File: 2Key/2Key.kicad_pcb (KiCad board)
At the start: 2 copper layers, 20 parts, among them SW1 SW_Push, U1 ATmega32U4-A, Y1 16MHz

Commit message: l
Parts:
- C1, C2, C3, C4, C5, C6, C7, F1, R1, R2, R3, R4, R5, R6, SW1, U1, USB1, Y1: moved to B.Cu
- moved R2 61.2 mm to (159.5, 65.1), turned to -90 degrees
- moved R3 60.5 mm to (162.7, 65.1), turned to -90 degrees
- moved F1 42.8 mm to (175.4, 101.6), turned to 180 degrees
- moved C3 37.2 mm to (179.0, 132.5), turned to 180 degrees
- moved C6 35.1 mm to (169.1, 101.0), turned to -90 degrees
- moved R4 30.1 mm to (151.6, 98.4), turned to -90 degrees
- moved C1 28.6 mm to (146.1, 99.9), turned to 180 degrees
- moved C2 28.6 mm to (146.1, 108.6), turned to 0 degrees
- moved Y1 28.6 mm to (146.1, 103.8), turned to 180 degrees
- moved R1 27.2 mm to (146.7, 123.2), turned to 180 degrees
- moved C4 26.0 mm to (173.3, 132.2), turned to 180 degrees
- moved C7 25.4 mm to (169.9, 108.0), turned to 90 degrees
- moved R5 18.4 mm to (151.2, 129.1), turned to 180 degrees
- moved R6 9.57 mm to (155.6, 129.2), turned to 180 degrees
- moved USB1 2.25 mm to (160.3, 55.6)
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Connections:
- C6 pad 1: +5V -> VCC
- C7 pad 1: +5V -> VCC
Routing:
- net Net-(R3-Pad2): track 0.00 -> 45.8 mm, vias 0 -> 2
- net Net-(R2-Pad2): track 0.00 -> 45.5 mm, vias 0 -> 2
- net Net-(R4-Pad2): track 0.00 -> 25.1 mm, vias 0 -> 2
- net Net-(C1-Pad2): track 0.00 -> 25.0 mm
- net GND: track 0.00 -> 24.5 mm
- net Net-(C2-Pad2): track 0.00 -> 11.8 mm
- net VCC: track 0.00 -> 7.22 mm
- net +5V: track 0.00 -> 3.67 mm

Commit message: Save Progress
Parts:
- added D1: WS2812B, LED_SMD:LED_WS2812B-2020_PLCC4_2.0x2.0mm, B.Cu at (169.9, 85.7)
- added D2: WS2812B, LED_SMD:LED_WS2812B-2020_PLCC4_2.0x2.0mm, F.Cu at (181.0, 112.7)
- added R7: 5.1k, Resistor_SMD:R_0805_2012Metric, B.Cu at (167.5, 61.1)
- added R8: 5.1k, Resistor_SMD:R_0805_2012Metric, B.Cu at (153.3, 61.1)
- added U2: PRTR5V0U2X, Package_TO_SOT_SMD:SOT-143, B.Cu at (160.3, 67.5)
- USB1: value Molex-0548190589 -> HRO-TYPE-C-31-M-12; footprint Connector_USB:USB_Micro-B_Molex-105133-0031 -> Type-C:HRO-TYPE-C-31-M-12-Assembly
- moved C3 46.2 mm to (154.0, 93.7), turned to 90 degrees
- moved R6 42.7 mm to (169.9, 88.9)
- moved R5 41.0 mm to (150.7, 88.1)
- moved F1 37.7 mm to (165.9, 65.1), turned to -90 degrees
- moved R1 33.7 mm to (166.7, 96.0), turned to 90 degrees
- moved C4 20.5 mm to (164.9, 113.5)
- moved R2 7.32 mm to (158.0, 72.2)
- moved R3 7.14 mm to (162.7, 72.2)
- moved USB1 3.37 mm to (160.3, 52.2)
- moved C5 0.65 mm to (160.3, 113.5)
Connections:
- C6 pad 1: VCC -> +5V
- C7 pad 1: VCC -> +5V
- MX1 pad 2: Net-(R5-Pad2) -> Net-(MX1-Pad2)
- MX2 pad 2: Net-(R6-Pad2) -> Net-(MX2-Pad2)
- R5 pad 2: Net-(R5-Pad2) -> Net-(MX1-Pad2)
- R6 pad 2: Net-(R6-Pad2) -> Net-(MX2-Pad2)
- U1 pad 25: unconnected-(U1-Pad25) -> Net-(MX1-Pad2)
- U1 pad 26: unconnected-(U1-Pad26) -> RGBLED
- U1 pad 32: unconnected-(U1-Pad32) -> Net-(MX2-Pad2)
- U1 pad 8: Net-(R5-Pad2) -> unconnected-(U1-Pad8)
- U1 pad 9: Net-(R6-Pad2) -> unconnected-(U1-Pad9)
- USB1 pad 2: unconnected-(USB1-Pad2) -> VCC
- USB1 pad 3: D+ -> unconnected-(USB1-Pad3)
- USB1 pad 4: D- -> Net-(R8-Pad1)
- USB1 pad 5: VCC -> D-
- USB1 pad 6: unconnected-(USB1-Pad6) -> D+
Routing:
- net +5V: track 3.67 -> 162.5 mm, vias 0 -> 4
- net Net-(MX2-Pad2): track 0.00 -> 32.5 mm, vias 0 -> 2
- net D+: track 0.00 -> 27.5 mm, vias 0 -> 2
- net Net-(MX1-Pad2): track 0.00 -> 26.2 mm, vias 0 -> 2
- net D-: track 0.00 -> 25.8 mm, vias 0 -> 4
- net Net-(R2-Pad2): track 45.5 -> 24.5 mm
- net VCC: track 7.22 -> 26.3 mm, vias 0 -> 3
- net Net-(C3-Pad1): track 0.00 -> 18.5 mm, vias 0 -> 2
- net Net-(R8-Pad1): track 0.00 -> 11.5 mm
- net Net-(R7-Pad1): track 0.00 -> 11.1 mm
- net Net-(R3-Pad2): track 45.8 -> 38.0 mm
- net GND: track 24.5 -> 29.5 mm
- net Net-(R1-Pad1): track 0.00 -> 3.23 mm

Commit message: Save Progress
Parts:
- D2: moved to B.Cu
- moved D2 29.2 mm to (169.9, 85.7), turned to 180 degrees
- moved D1 19.2 mm to (150.7, 85.7)
- moved R5 0.79 mm to (150.7, 88.9)
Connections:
- U1 pad 14: VCC -> +5V
- U1 pad 2: VCC -> +5V
- U1 pad 24: VCC -> +5V
- U1 pad 44: VCC -> +5V
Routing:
- net Net-(D1-Pad2): track 0.00 -> 20.2 mm, vias 0 -> 6
- net RGBLED: track 0.00 -> 19.5 mm, vias 0 -> 2
- net GND: track 29.5 -> 44.4 mm, vias 0 -> 3
- net Net-(R2-Pad2): track 24.5 -> 39.0 mm
- net Net-(MX1-Pad2): track 26.2 -> 35.5 mm
- net +5V: track 162.5 -> 153.9 mm, vias 4 -> 2
- net Net-(R3-Pad2): track 38.0 -> 38.6 mm

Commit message: Updated PCB
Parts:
- added C8: 0.1uF, Capacitor_SMD:C_0805_2012Metric, B.Cu at (151.2, 109.0)
- added C9: 0.1uF, Capacitor_SMD:C_0805_2012Metric, B.Cu at (153.8, 96.8)
- MX1, MX2: moved to B.Cu
- moved C3 20.0 mm to (156.8, 113.5), turned to 180 degrees
- moved R4 1.11 mm to (150.5, 98.5)
- turned MX1 to 180 degrees
- turned MX2 to 180 degrees
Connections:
- U1 pad 34: VCC -> +5V
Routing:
- net GND: track 44.4 -> 119.4 mm, vias 3 -> 14
- net +5V: track 153.9 -> 180.0 mm, vias 2 -> 6
- net Net-(C3-Pad1): track 18.5 -> 5.59 mm
- net Net-(MX2-Pad2): track 32.5 -> 28.4 mm, vias 2 -> 3
- net Net-(R4-Pad2): track 25.1 -> 27.1 mm
- net VCC: track 26.3 -> 27.2 mm
- net D-: track 25.8 -> 25.0 mm
- net Net-(R3-Pad2): track 38.6 -> 39.3 mm
- net Net-(MX1-Pad2): track 35.5 -> 35.6 mm, vias 2 -> 3
- added copper zone on B.Cu, net GND
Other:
- board outline added: 49.2 x 71.4 mm

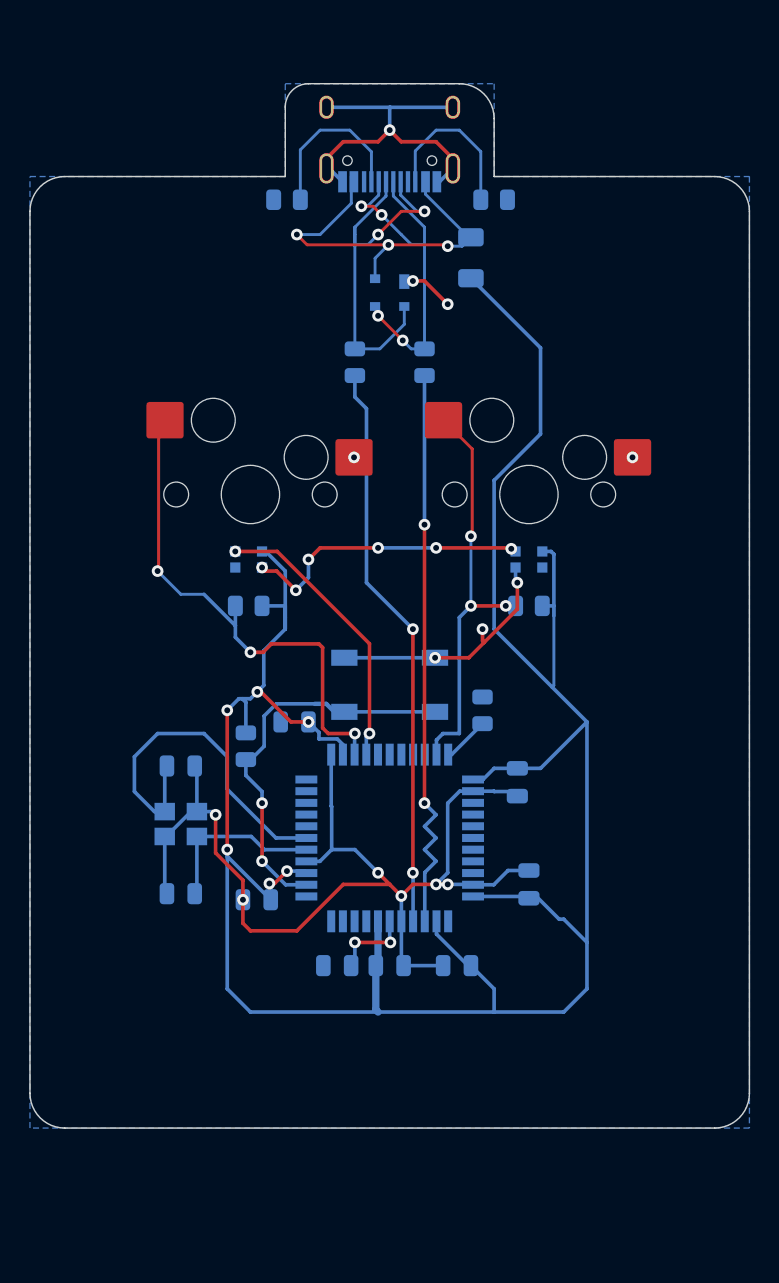
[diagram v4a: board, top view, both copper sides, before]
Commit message: Remade PCB with the MU Chip
Remade the PCB with the MU Chip and switched to reverse mounted LEDs
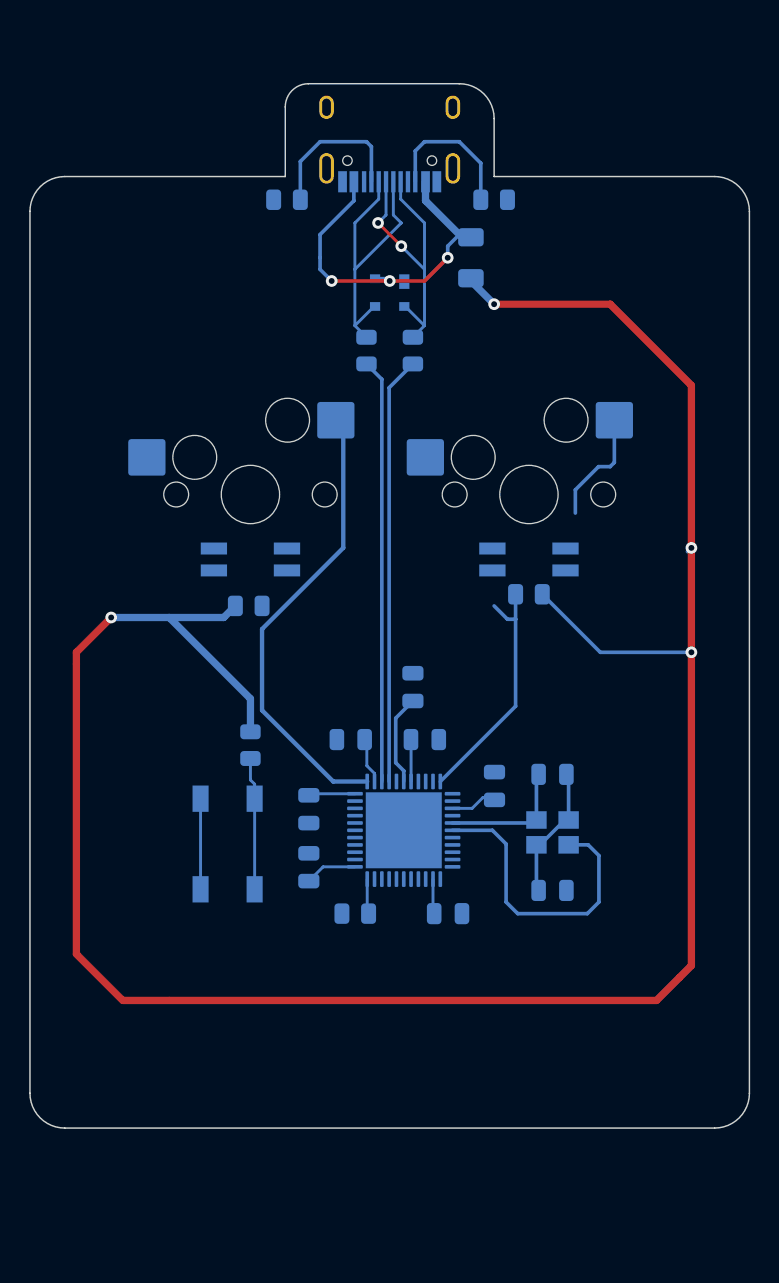
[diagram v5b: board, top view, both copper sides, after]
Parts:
- C3: value C_Small -> 1uF
- D1, D2: value WS2812B -> SK6812MINI; footprint LED_SMD:LED_WS2812B-2020_PLCC4_2.0x2.0mm -> LED:SK6812MINIE
- MX1, MX2: moved to F.Cu
- U1: value ATmega32U4-A -> ATmega32U4-M; footprint Package_QFP:TQFP-44_10x10mm_P0.8mm -> Package_DFN_QFN:QFN-44-1EP_7x7mm_P0.5mm_EP5.2x5.2mm
- moved C1 26.8 mm to (171.5, 108.4), turned to 0 degrees
- moved C2 26.7 mm to (171.5, 100.4), turned to 180 degrees
- moved Y1 25.4 mm to (171.5, 104.4), turned to 0 degrees
- moved C3 19.7 mm to (161.9, 94.5), turned to 90 degrees
- moved R1 16.4 mm to (158.0, 110.0), turned to 180 degrees
- moved C7 15.9 mm to (154.8, 102.8), turned to -90 degrees
- moved C5 15.6 mm to (162.7, 98.0)
- moved SW1 15.5 mm to (149.2, 105.2), turned to -90 degrees
- moved C9 14.4 mm to (167.5, 101.2), turned to 90 degrees
- moved C6 11.8 mm to (157.7, 98.0), turned to 180 degrees
- moved C8 4.19 mm to (154.8, 106.8), turned to 90 degrees
- moved R2 4.05 mm to (161.9, 71.4)
- moved R3 4.05 mm to (158.8, 71.4)
- moved C4 3.61 mm to (164.3, 110.0), turned to 0 degrees
- moved U1 1.10 mm to (161.3, 104.2), turned to -90 degrees
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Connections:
- D1 pad 1: +5V -> Net-(D1-Pad1)
- D1 pad 2: Net-(D1-Pad2) -> GND
- D1 pad 3: GND -> RGBLED
- D1 pad 4: RGBLED -> +5V
- D2 pad 1: +5V -> unconnected-(D2-Pad1)
- D2 pad 2: unconnected-(D2-Pad2) -> GND
- D2 pad 3: GND -> Net-(D1-Pad1)
- D2 pad 4: Net-(D1-Pad2) -> +5V
- U1 pad 1: unconnected-(U1-Pad1) -> Net-(MX2-Pad2)
- U1 pad 11: unconnected-(U1-Pad11) -> Net-(MX1-Pad2)
- U1 pad 14: +5V -> VCC
- U1 pad 2: +5V -> VCC
- U1 pad 24: +5V -> VCC
- U1 pad 25: Net-(MX1-Pad2) -> unconnected-(U1-Pad25)
- U1 pad 32: Net-(MX2-Pad2) -> unconnected-(U1-Pad32)
- U1 pad 34: +5V -> VCC
- U1 pad 44: +5V -> VCC
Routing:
- net GND: track 119.4 -> 15.5 mm, vias 14 -> 0
- net Net-(D1-Pad2): track 20.2 -> 0.00 mm, vias 6 -> 0
- net RGBLED: track 19.5 -> 0.00 mm, vias 2 -> 0
- net Net-(R4-Pad2): track 27.1 -> 9.07 mm, vias 2 -> 0
- net +5V: track 180.0 -> 165.9 mm, vias 6 -> 4
- net Net-(R3-Pad2): track 39.3 -> 29.0 mm, vias 2 -> 0
- net Net-(R2-Pad2): track 39.0 -> 29.2 mm, vias 2 -> 0
- net VCC: track 27.2 -> 35.9 mm
- net D+: track 27.5 -> 21.3 mm
- net Net-(C1-Pad2): track 24.9 -> 20.8 mm
- net Net-(MX1-Pad2): track 35.6 -> 31.6 mm, vias 3 -> 0
- net D-: track 25.0 -> 21.1 mm, vias 4 -> 0
- net Net-(MX2-Pad2): track 28.4 -> 24.7 mm, vias 3 -> 0
- net Net-(C2-Pad2): track 11.8 -> 9.00 mm
- net Net-(R7-Pad1): track 11.1 -> 9.96 mm
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- removed copper zone on B.Cu, net GND

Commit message: Update
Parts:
- moved R6 1.59 mm to (169.9, 89.7)
- moved R5 0.79 mm to (150.7, 89.7)
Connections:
- U1 pad 1: Net-(MX2-Pad2) -> Net-(MX1-Pad2)
- U1 pad 11: Net-(MX1-Pad2) -> Net-(MX2-Pad2)
- U1 pad 14: VCC -> +5V
- U1 pad 2: VCC -> +5V
- U1 pad 24: VCC -> +5V
- U1 pad 34: VCC -> +5V
- U1 pad 44: VCC -> +5V
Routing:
- net +5V: track 165.9 -> 275.0 mm, vias 4 -> 9
- net GND: track 15.5 -> 98.9 mm, vias 0 -> 10
- net RGBLED: track 0.00 -> 51.6 mm, vias 0 -> 2
- net Net-(R4-Pad2): track 9.07 -> 27.8 mm, vias 0 -> 2
- net Net-(D1-Pad1): track 0.00 -> 14.7 mm, vias 0 -> 2
- net Net-(MX2-Pad2): track 24.7 -> 39.4 mm
- net VCC: track 35.9 -> 26.0 mm
- net Net-(MX1-Pad2): track 31.6 -> 35.0 mm
- net Net-(C1-Pad2): track 20.8 -> 23.8 mm
- added copper zone on B.Cu, net GND
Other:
- outline, holes or cut-outs redrawn
